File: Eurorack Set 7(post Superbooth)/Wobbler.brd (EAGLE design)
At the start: 59.6 x 106.5 mm, 127 parts, among them IC1 LD1117AS33TR, IC3 TL074D, IC4 MCP6004, J1 PJ-341, J12 PJ-341, J13 PJ-341, J14 POWERSMT, J2 PJ-341, J3 PJ-341, J4 PJ-341, J5 PJ-341, J6 PJ-341, J7 PJ-341, J8 PJ-341, Q1 MMBT3904, Q2 MMBT3904, Q3 MMBT3904, Q5 MMBT3904, U1 MKL02Z32VFK4, U2 LM4040DIM3-5.0, U4 74HC595BQ, U5 74HC595BQ, U6 24LC16T-I/OT, U7 MCP4822-E/SN

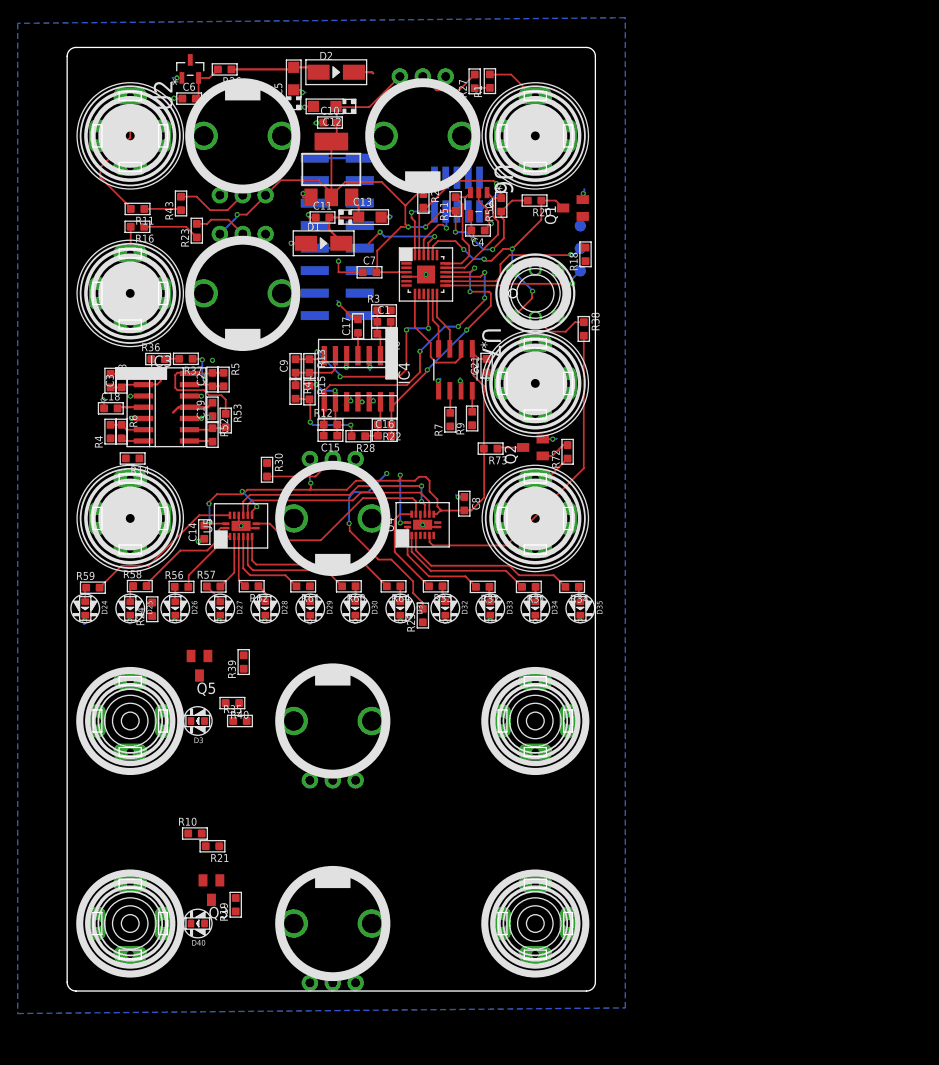
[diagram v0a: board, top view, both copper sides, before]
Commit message: EnvFollower values, bigfish fixes, wobbler updates, lineout clarifications
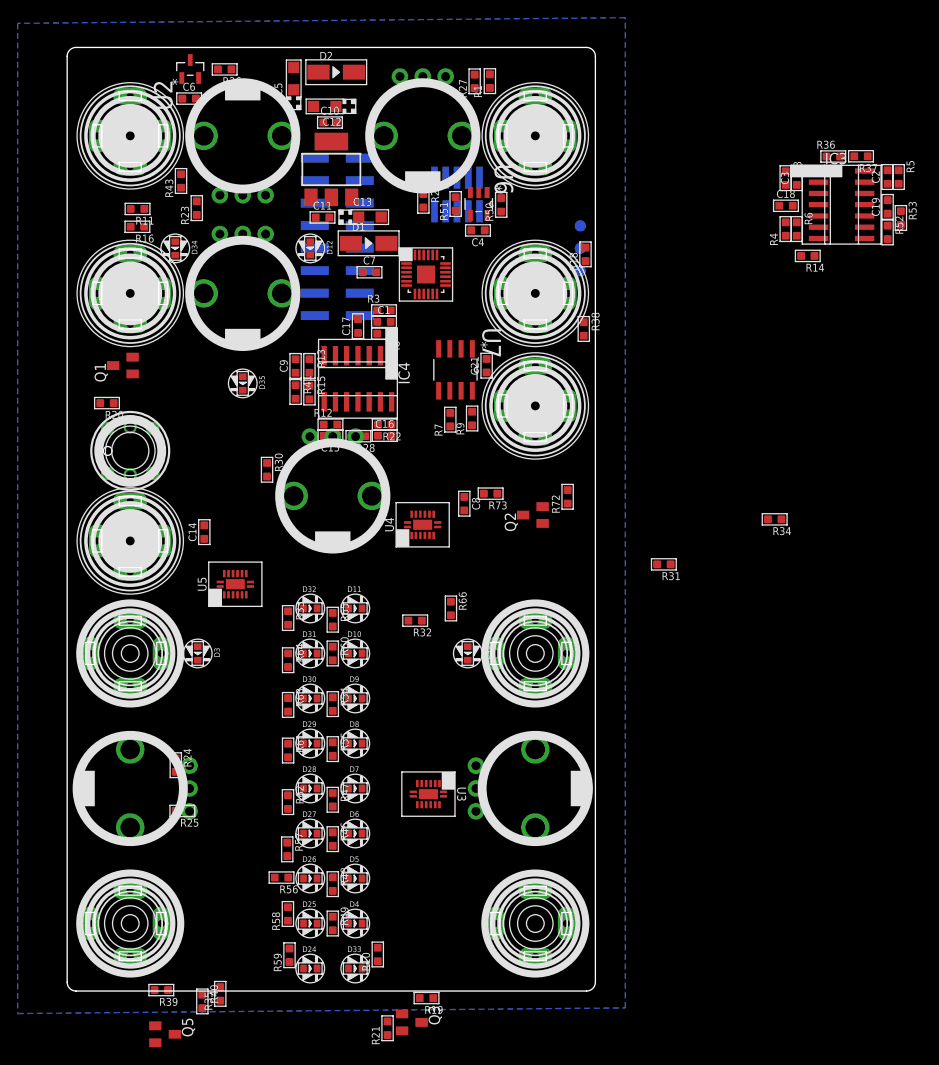
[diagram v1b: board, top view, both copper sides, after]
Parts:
- added D10, D11, D12, D4, D5, D6, D7, D8, D9: yellow, EurorackModularParts:LED0603
- added R46, R47, R48, R49, R54, R55, R60, R65, R66: 56, OPL:R0603
- added U3: 74HC595BQ, FarnellThings:QFN50P250X350X100-17N
- moved C18 79.6 mm to (81.6, 88.6)
- moved R36 79.6 mm to (87.0, 94.2)
- moved R37 79.6 mm to (90.1, 94.2)
- moved C19 79.6 mm to (93.1, 88.5)
- moved C2 79.6 mm to (93.1, 91.9)
- moved C3 79.6 mm to (82.8, 91.8)
- moved IC3 79.6 mm to (87.9, 88.8)
- moved R14 79.6 mm to (84.1, 83.0)
- moved R4 79.6 mm to (81.6, 86.0)
- moved R5 79.6 mm to (94.3, 91.9)
- moved R52 79.6 mm to (93.1, 85.6)
- moved R53 79.6 mm to (94.6, 87.3)
- moved R6 79.6 mm to (82.8, 86.0)
- moved R8 79.6 mm to (81.6, 91.8)
- moved D34 57.5 mm to (12.7, 83.8)
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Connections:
- new net ADC_NORMAL: R44.P$2
- new net ADC_PHASED: R45.P$2
- new net N$14: D7.+, R47.1
- new net N$46: D6.+, R46.1
- new net N$47: D5.+, R48.1
- new net N$48: D4.+, R49.1
- new net N$49: D8.+, R55.1
- new net N$50: D9.+, R54.1
- new net N$51: D10.+, R60.1
- new net N$52: D11.+, R65.1
- new net N$53: R49.2, U3.15
- new net N$54: R48.2, U3.1
- new net N$55: R46.2, U3.2
- new net N$56: R47.2, U3.3
- new net N$57: R55.2, U3.4
- new net N$58: R54.2, U3.5
- new net N$59: R60.2, U3.6
- new net N$62: R65.2, U3.7
- new net N$63: R66.2, U4.7
- new net N$65: D12.+, R66.1
- new net SHIFTERS2TO3: U3.14, U4.9
- net 3.3V: now also R44.P$3, R45.P$3, U3.10, U3.16
- net CLOCK: now also U3.11
- net GND: now also D10.-, D11.-, D12.-, D4.-, D5.-, D6.-, D7.-, D8.-, D9.-, R44.P$1, R45.P$1, U3.13, U3.17, U3.8
- net LATCH: now also U3.12
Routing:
- net 3.3V: track 167.5 -> 0.00 mm, vias 14 -> 0
- net GND: track 66.9 -> 0.00 mm, vias 44 -> 0
- net TRIGGERBUTTONLED: track 36.9 -> 0.00 mm
- net ADC_SHAPE: track 36.5 -> 0.00 mm, vias 4 -> 0
- net RESET_PATTERN: track 31.1 -> 0.00 mm, vias 4 -> 0
- net ADC_FREQ: track 30.1 -> 0.00 mm, vias 4 -> 0
- net ADC_PHASE: track 27.0 -> 0.00 mm, vias 5 -> 0
- net LATCH: track 25.7 -> 0.00 mm, vias 2 -> 0
- net PHASEDOUT: track 25.0 -> 0.00 mm, vias 2 -> 0
- net CLOCK: track 24.1 -> 0.00 mm
- net SHIFTER1TO2: track 22.4 -> 0.00 mm
- net N$36: track 20.3 -> 0.00 mm
- net N$40: track 19.1 -> 0.00 mm
- net CPU_RESET: track 19.1 -> 0.00 mm, vias 1 -> 0
- net N$22: track 18.1 -> 0.00 mm
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
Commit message: LOTS of updates..... JUNE2017 prototype sprint!
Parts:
- removed GNDPIN, TX: TPB1,27, testpad:B1,27
- added C20: 100nF, OPL:C0603
- D10, D11, D12, D24, D25, D26, D27, D28, D29, D3, D30, D31, D32, D33, D34, D35, D4, D40, D5, D6, D7, D8, D9: device EurorackModularParts:LED0603 -> EurorackModularParts:3MMLED
- moved R14 76.8 mm to (13.4, 53.0), turned to 270 degrees
- moved U2 60.9 mm to (41.5, 49.5)
- moved R34 56.6 mm to (34.7, 86.7), turned to 0 degrees
- moved C6 55.8 mm to (41.5, 52.0)
- moved R31 53.6 mm to (23.0, 77.5), turned to 270 degrees
- moved R26 52.6 mm to (40.6, 56.4), turned to 270 degrees
- moved R38 52.0 mm to (31.2, 30.7), turned to 0 degrees
- moved J1 48.8 mm to (7.62, 48.9)
- moved C7 47.3 mm to (26.8, 34.5), turned to 90 degrees
- moved J5 45.8 mm to (53.3, 48.9)
- moved R25 45.5 mm to (58.4, 13.2), turned to 90 degrees
- moved SWD1 44.4 mm to (16.6, 55.4), turned to 0 degrees
- moved R4 43.8 mm to (44.5, 62.8)
- moved R20 43.6 mm to (45.6, 50.4), turned to 270 degrees
- moved R6 43.6 mm to (46.0, 62.8)
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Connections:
- removed net N$30 (its old number): R58.2, U5.1
- removed net N$59 (its old number): R60.2, U3.6
- removed net N$63: R66.2, U4.7
- new net N$26: R61.2, U5.3
- new net N$37: R59.2, U4.3
- net 3.3V: now also C20.2
- net ADC_NORMAL: now also U1.9
- net ADC_PHASED: now also U1.14
- net GND: now also C20.1; no longer GNDPIN.TP
- net N$1: now also U5.15; no longer U4.15
- net N$19: now also R64.2, U5.1; no longer R32.2, U4.1
- net N$22: now also R63.2, U5.2; no longer R59.2, U5.15
- net N$31: now also R57.2, U5.5; no longer R56.2, U5.2
- net N$35: now also R56.2, U5.6; no longer R57.2, U5.3
- net N$36: now also R58.2, U5.7; no longer R34.2, U4.3
- net N$38: now also R54.2, U3.7; no longer R61.2, U5.5
- net N$39: now also R55.2, U3.6; no longer R63.2, U5.6
- net N$40: now also R47.2, U3.5; no longer R64.2, U5.7
- net N$43: now also R46.2, U3.4; no longer TX.TP, U1.14
- net N$53: now also R48.2, U3.3; no longer R49.2, U3.15
- net N$54: now also R49.2, U3.2; no longer R48.2, U3.1
- net N$55: now also R32.2, U3.1; no longer R46.2, U3.2
- net N$56: now also R65.2, U3.15; no longer R47.2, U3.3
- net N$57: now also R60.2, U4.7; no longer R55.2, U3.4
- net N$58: now also R34.2, U4.1; no longer R54.2, U3.5
- net N$62: now also R66.2, U4.15; no longer R65.2, U3.7
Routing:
- net 3.3V: track 0.00 -> 327.8 mm, vias 0 -> 24
- net 12V: track 0.00 -> 173.0 mm, vias 0 -> 6
- net RESET_PATTERN: track 0.00 -> 161.5 mm, vias 0 -> 10
- net REF_-5V: track 0.00 -> 132.5 mm, vias 0 -> 11
- net NORMALOUT: track 0.00 -> 122.2 mm, vias 0 -> 4
- net N$8: track 0.00 -> 93.4 mm
- net ADC_PHASED: track 0.00 -> 78.5 mm, vias 0 -> 6
- net LATCH: track 0.00 -> 78.1 mm, vias 0 -> 14
- net OUT_LFOCYCLEMID: track 0.00 -> 69.7 mm, vias 0 -> 2
- net CLOCK: track 0.00 -> 66.4 mm, vias 0 -> 7
- net N$58: track 0.00 -> 64.5 mm, vias 0 -> 2
- net ADC_NORMAL: track 0.00 -> 61.5 mm, vias 0 -> 2
- net GND: track 0.00 -> 61.1 mm, vias 0 -> 39
- net N$59: track 0.00 -> 59.4 mm, vias 0 -> 6
- net PHASEDOUT: track 0.00 -> 54.5 mm
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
